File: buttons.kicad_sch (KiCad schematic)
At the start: 24 parts, among them SW10 SW_Push, SW3 SW_Push, SW4 SW_Push, SW5 SW_Push, SW6 SW_Push, SW7 SW_Push, SW8 SW_Push, SW9 SW_Push

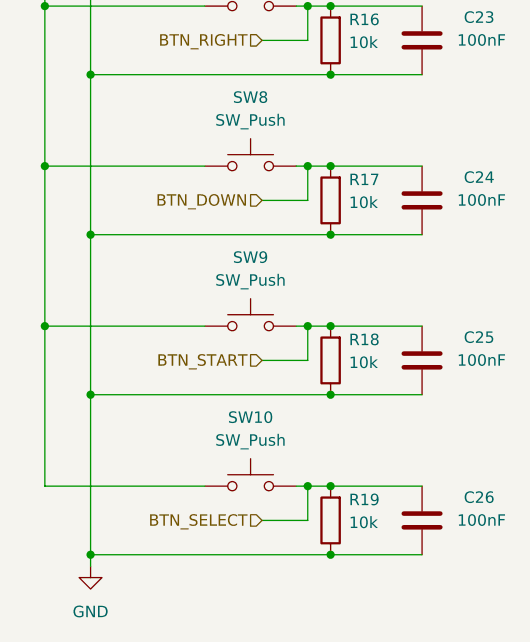
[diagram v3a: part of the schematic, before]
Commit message: check with hardware manual, add comments, add mpns
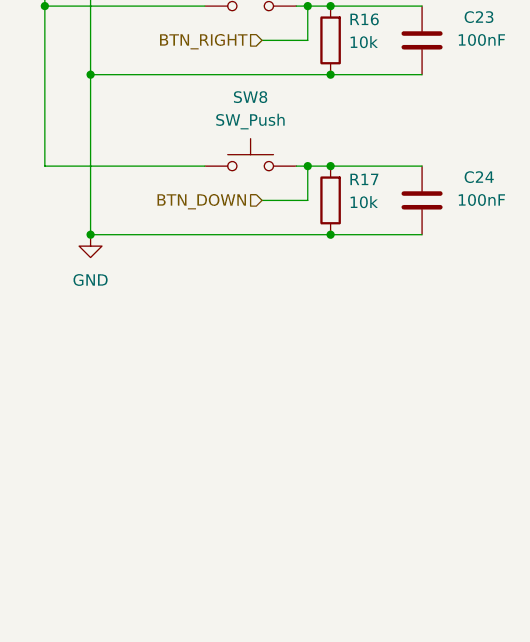
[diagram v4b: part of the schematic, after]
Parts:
- removed C25, C26: 100nF, Capacitor_SMD:C_0603_1608Metric, symbol Device:C
- removed R18, R19: 10k, Resistor_SMD:R_0603_1608Metric, symbol Device:R
- removed SW10, SW9: SW_Push, Button_Switch_SMD:SW_Push_1TS009xxxx-xxxx-xxxx_6x6x5mm, symbol Switch:SW_Push

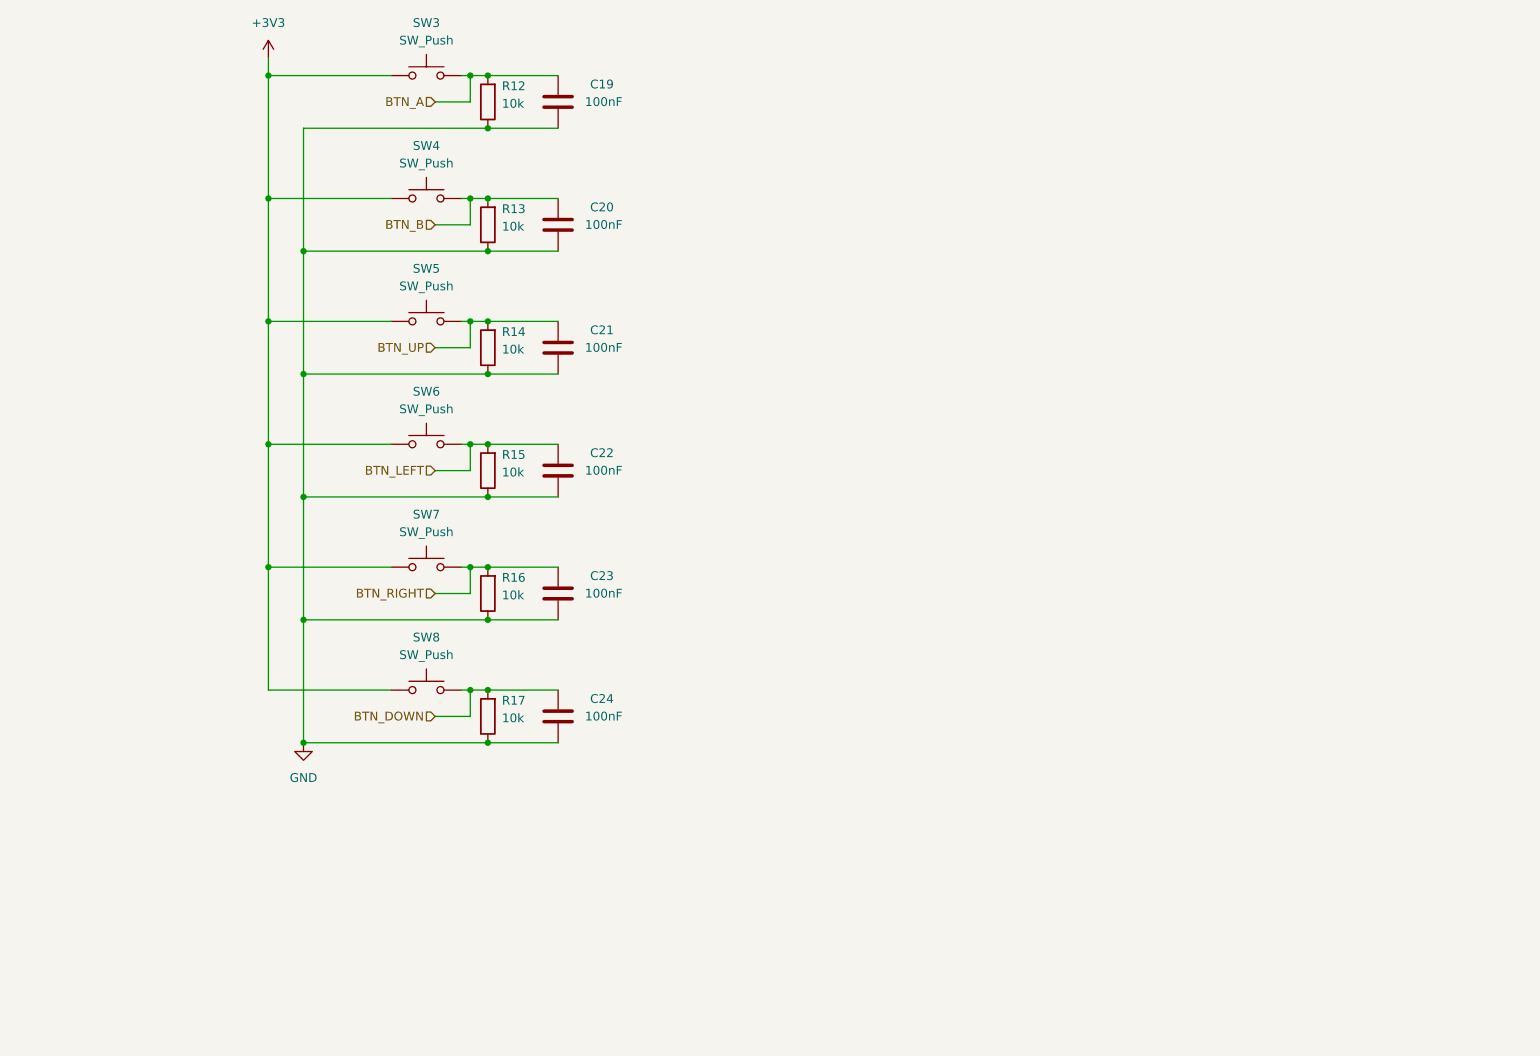
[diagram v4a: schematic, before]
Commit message: fix usb and add esd diodes, some other checks
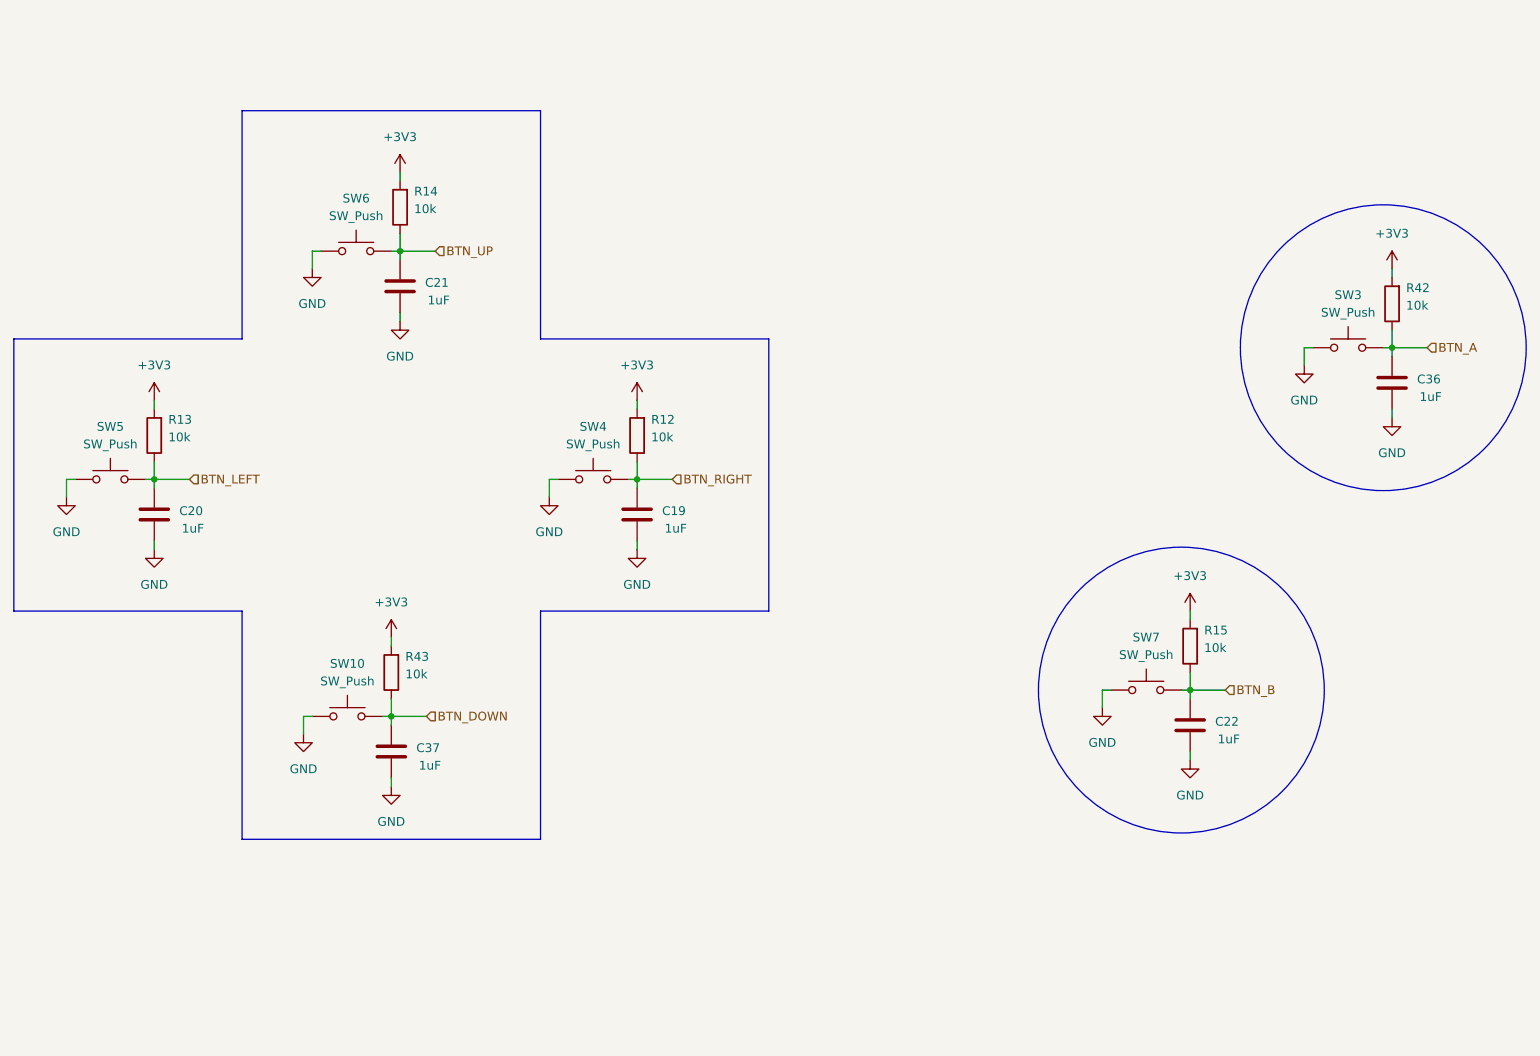
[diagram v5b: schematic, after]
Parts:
- removed C23, C24: 100nF, Capacitor_SMD:C_0603_1608Metric, symbol Device:C
- removed R16, R17: 10k, Resistor_SMD:R_0603_1608Metric, symbol Device:R
- removed SW8: SW_Push, Button_Switch_SMD:SW_Push_1TS009xxxx-xxxx-xxxx_6x6x5mm, symbol Switch:SW_Push
- added C36, C37: 1uF, Capacitor_SMD:C_0603_1608Metric, symbol Device:C
- added R42, R43: 10k, Resistor_SMD:R_0603_1608Metric, symbol Device:R
- added SW10: SW_Push, Button_Switch_SMD:SW_Push_1TS009xxxx-xxxx-xxxx_6x6x5mm, symbol Switch:SW_Push
- C19, C20, C21, C22: value 100nF -> 1uF
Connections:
- net +3V3: now also R12.2, R13.2, R14.2, R15.2, R42.2, R43.2; no longer SW3.1, SW4.1, SW5.1, SW6.1, SW7.1
- net BTN_A: now also C36.2, R42.1; no longer C19.2, R12.2
- net BTN_B: now also C22.2, R15.1, SW7.2; no longer C20.2, R13.2, SW4.2
- net BTN_DOWN: now also C37.2, R43.1, SW10.2
- net BTN_LEFT: now also C20.2, R13.1, SW5.2; no longer C22.2, R15.2, SW6.2
- net BTN_RIGHT: now also C19.2, R12.1, SW4.2; no longer SW7.2
- net BTN_UP: now also R14.1, SW6.2; no longer R14.2, SW5.2
- net GND: now also SW3.1, SW4.1, SW5.1, SW6.1, SW7.1, C36.1, C37.1, SW10.1; no longer R12.1, R13.1, R14.1, R15.1
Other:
- moved on the sheet: SW3

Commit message: remove redundant passive lcsc numbers
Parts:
- C19, C20, C21, C22, C36, C37: LCSC C36508 -> (none)
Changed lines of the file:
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@@
 			)
 		)
-		(property "LCSC" "C36508"
+		(property "LCSC" ""
 			(at 87.63 138.43 0)
 			(effects
@@
 			)
 		)
-		(property "LCSC" "C36508"
+		(property "LCSC" ""
 			(at 123.19 104.14 0)
 			(effects
@@
 			)
 		)
-		(property "LCSC" "C36508"
+		(property "LCSC" ""
 			(at 53.34 104.14 0)
 			(effects
@@
 			)
 		)
-		(property "LCSC" "C36508"
+		(property "LCSC" ""
 			(at 232.41 85.09 0)
 			(effects
@@
 			)
 		)
-		(property "LCSC" "C36508"
+		(property "LCSC" ""
 			(at 203.2 134.62 0)
 			(effects
@@
 			)
 		)
-		(property "LCSC" "C36508"
+		(property "LCSC" ""
 			(at 88.9 71.12 0)
 			(effects

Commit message: align some components with inventory
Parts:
- C19, C20, C21, C22, C36, C37: footprint Capacitor_SMD:C_0603_1608Metric -> Capacitor_SMD:C_0402_1005Metric
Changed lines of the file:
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@@
 			)
 		)
-		(property "Footprint" "Capacitor_SMD:C_0603_1608Metric"
+		(property "Footprint" "Capacitor_SMD:C_0402_1005Metric"
 			(at 86.6648 134.62 0)
 			(effects
@@
 			)
 		)
-		(property "Footprint" "Capacitor_SMD:C_0603_1608Metric"
+		(property "Footprint" "Capacitor_SMD:C_0402_1005Metric"
 			(at 122.2248 100.33 0)
 			(effects
@@
 			)
 		)
-		(property "Footprint" "Capacitor_SMD:C_0603_1608Metric"
+		(property "Footprint" "Capacitor_SMD:C_0402_1005Metric"
 			(at 52.3748 100.33 0)
 			(effects
@@
 			)
 		)
-		(property "Footprint" "Capacitor_SMD:C_0603_1608Metric"
+		(property "Footprint" "Capacitor_SMD:C_0402_1005Metric"
 			(at 231.4448 81.28 0)
 			(effects
@@
 			)
 		)
-		(property "Footprint" "Capacitor_SMD:C_0603_1608Metric"
+		(property "Footprint" "Capacitor_SMD:C_0402_1005Metric"
 			(at 202.2348 130.81 0)
 			(effects
@@
 			)
 		)
-		(property "Footprint" "Capacitor_SMD:C_0603_1608Metric"
+		(property "Footprint" "Capacitor_SMD:C_0402_1005Metric"
 			(at 87.9348 67.31 0)
 			(effects
